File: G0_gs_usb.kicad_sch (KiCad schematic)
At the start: 54 parts, among them J1 USB_C_Receptacle_USB2.0, J12 CAN1, J13 CAN2, J4 Conn_01x03_Pin, U1 STM32G0B1CBTx, U2 TJA1042T-3, U3 TJA1042T-3, U4 XC6206PxxxMR

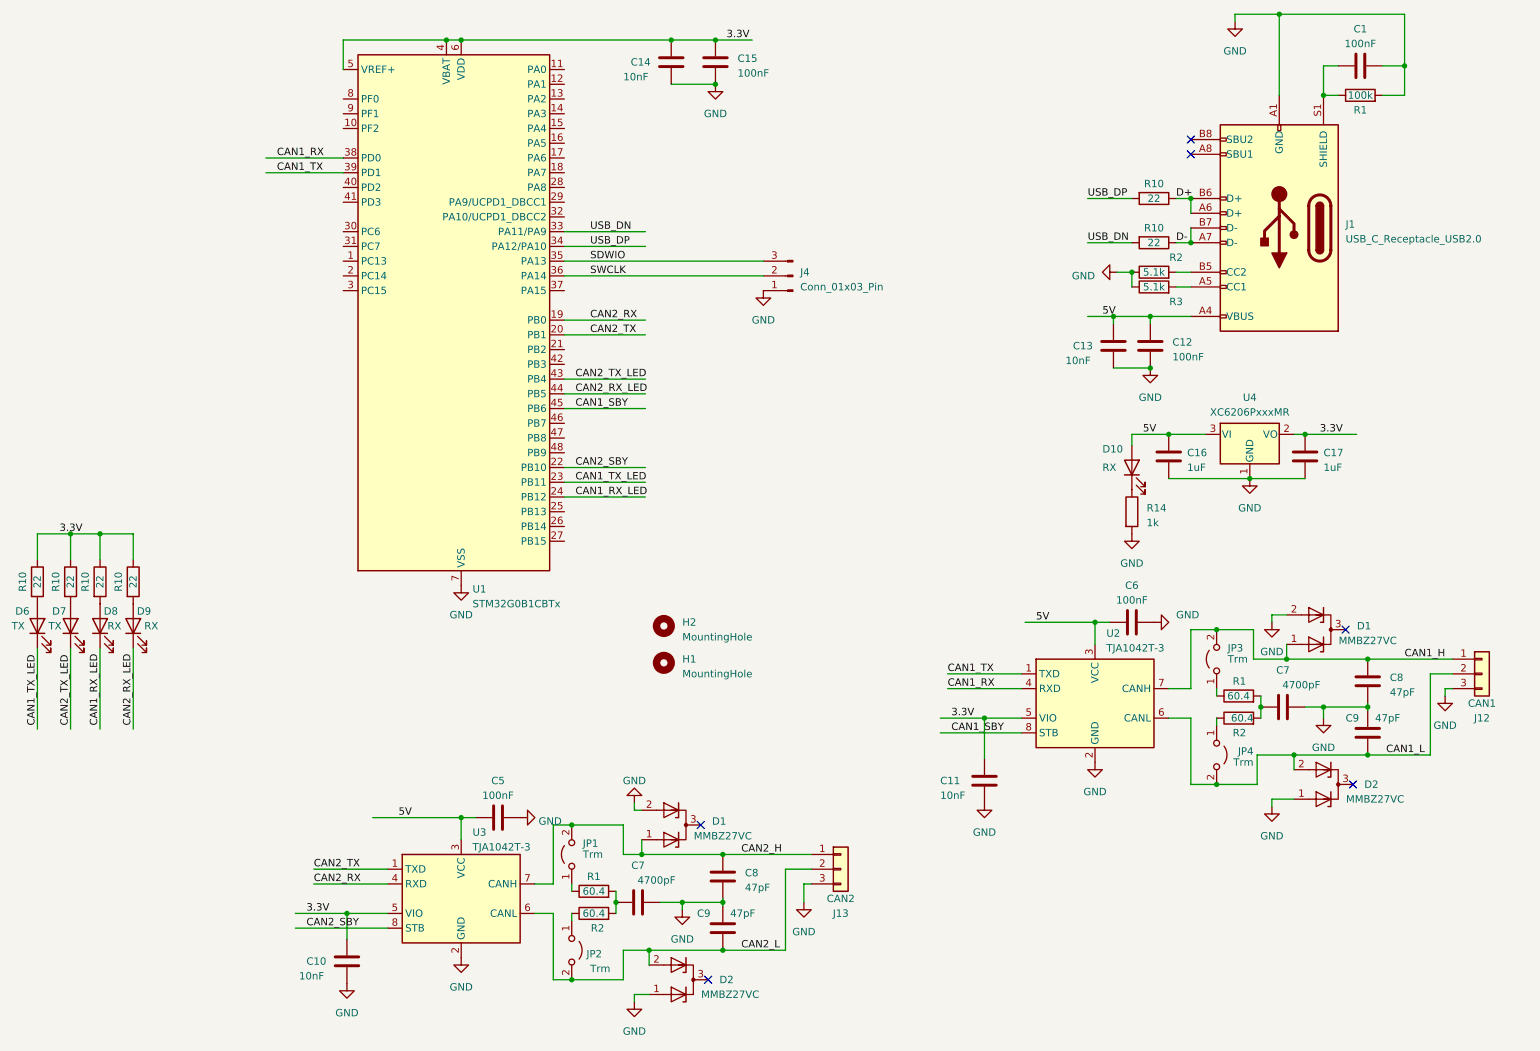
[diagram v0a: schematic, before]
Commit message: Update footprints on R and C to 0402. Added 5V protection. Routed CAN RX/TX as diff pairs.
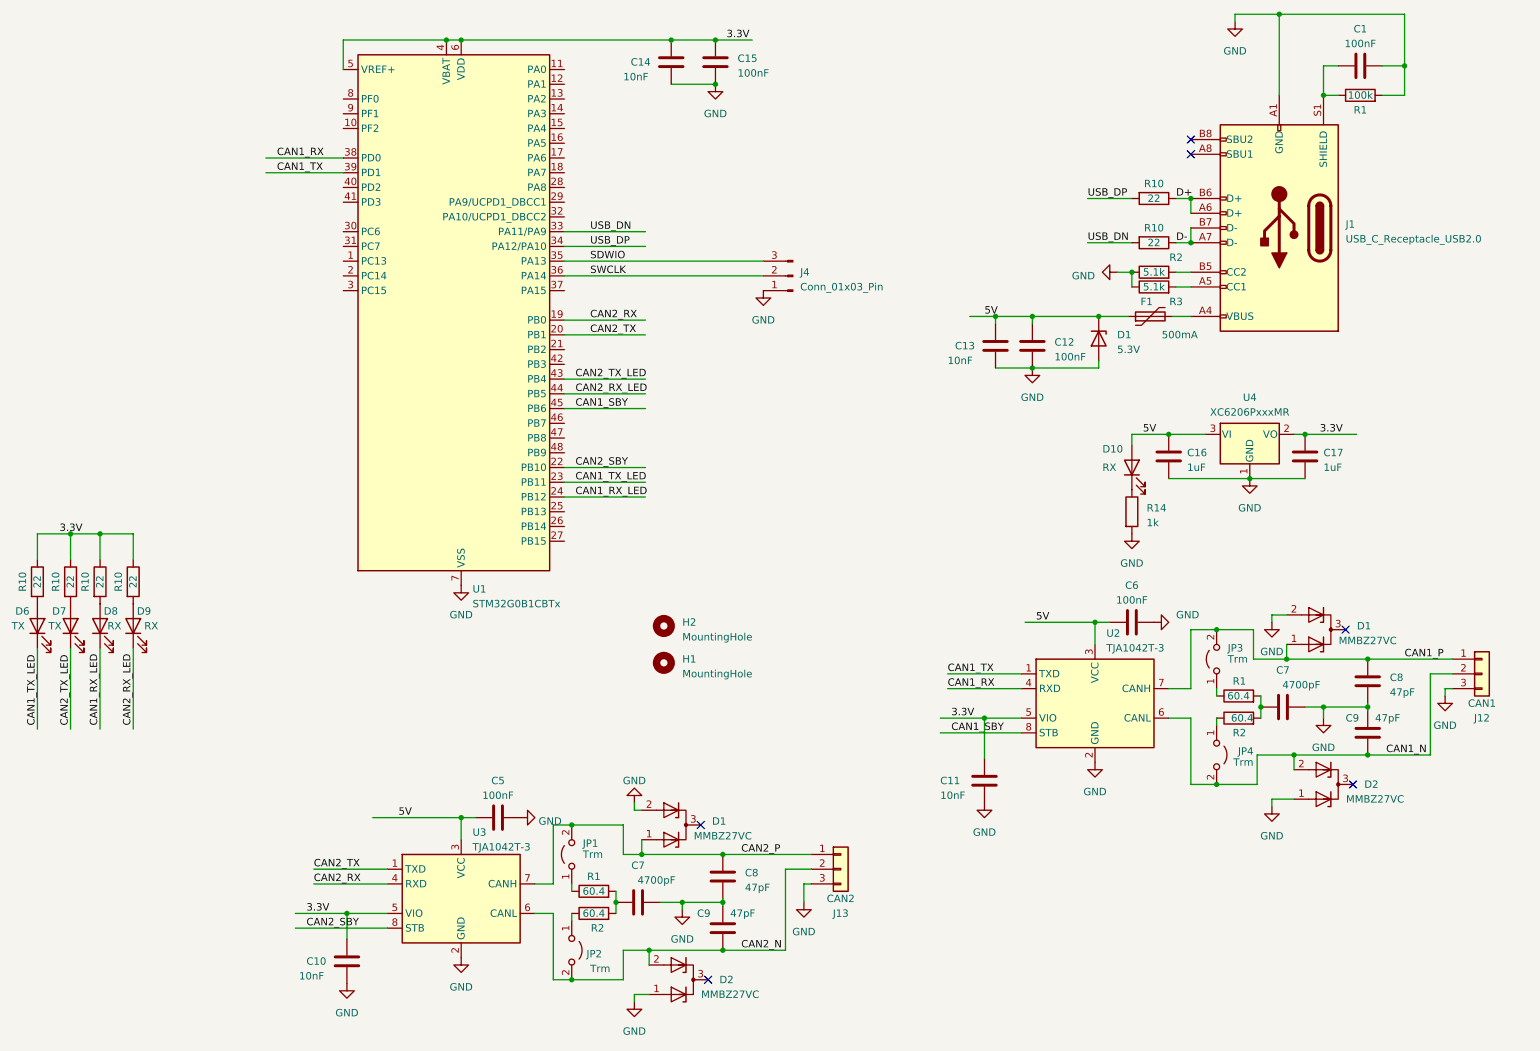
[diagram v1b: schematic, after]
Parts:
- added D1: 5.3V, Diode_SMD:D_MELF, symbol Device:D_Zener
- added F1: 500mA, Fuse:Fuse_0603_1608Metric, symbol Device:Polyfuse
- C1, C12, C15, C5, C6: footprint Capacitor_SMD:C_0603_1608Metric -> Capacitor_SMD:C_0402_1005Metric; LCSC Part # C14663 -> C307331; Part # (none) -> CL05B104KB54PNC
- C10, C11, C13, C14: footprint Capacitor_SMD:C_0603_1608Metric -> Capacitor_SMD:C_0402_1005Metric; LCSC Part # C57112 -> C15195; Part # (none) -> CL05B103KB5NNNC
- C7: footprint Capacitor_SMD:C_0603_1608Metric -> Capacitor_SMD:C_0402_1005Metric; LCSC Part # C53987 -> C1538; Part # (none) -> 0402B472K500NT
- C8, C9: footprint Capacitor_SMD:C_0603_1608Metric -> Capacitor_SMD:C_0402_1005Metric; LCSC Part # C1671 -> C1567; Part # (none) -> 0402CG470J500NT
- R1, R2: footprint Resistor_SMD:R_0603_1608Metric -> Resistor_SMD:R_0402_1005Metric; LCSC Part # C23090 -> C11616; Part # (none) -> 0402WGF5103TCE
- R1: footprint Resistor_SMD:R_0603_1608Metric -> Resistor_SMD:R_0402_1005Metric; LCSC Part # C25803 -> C11616; Part # (none) -> 0402WGF5103TCE
- R10: footprint Resistor_SMD:R_0603_1608Metric -> Resistor_SMD:R_0402_1005Metric; LCSC Part # C23345 -> C25092; Part # 0603WAF220JT5E -> 0402WGF220JTCE
- R2, R3: footprint Resistor_SMD:R_0603_1608Metric -> Resistor_SMD:R_0402_1005Metric; LCSC Part # C23186 -> C11616; Part # (none) -> 0402WGF5103TCE
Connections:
- net 5V: now also D1.1 (K), F1.1; no longer J1.A4 (VBUS), J1.A9 (VBUS), J1.B4 (VBUS), J1.B9 (VBUS)
- net GND: now also D1.2 (A)
- net CAN1_H renamed CAN1_P
- net CAN1_L renamed CAN1_N
- net CAN2_H renamed CAN2_P
- net CAN2_L renamed CAN2_N
- new net: F1.2, J1.A4 (VBUS), J1.A9 (VBUS), J1.B4 (VBUS), J1.B9 (VBUS)
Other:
- moved on the sheet: C12, C13

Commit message: Use better TVS diodes.
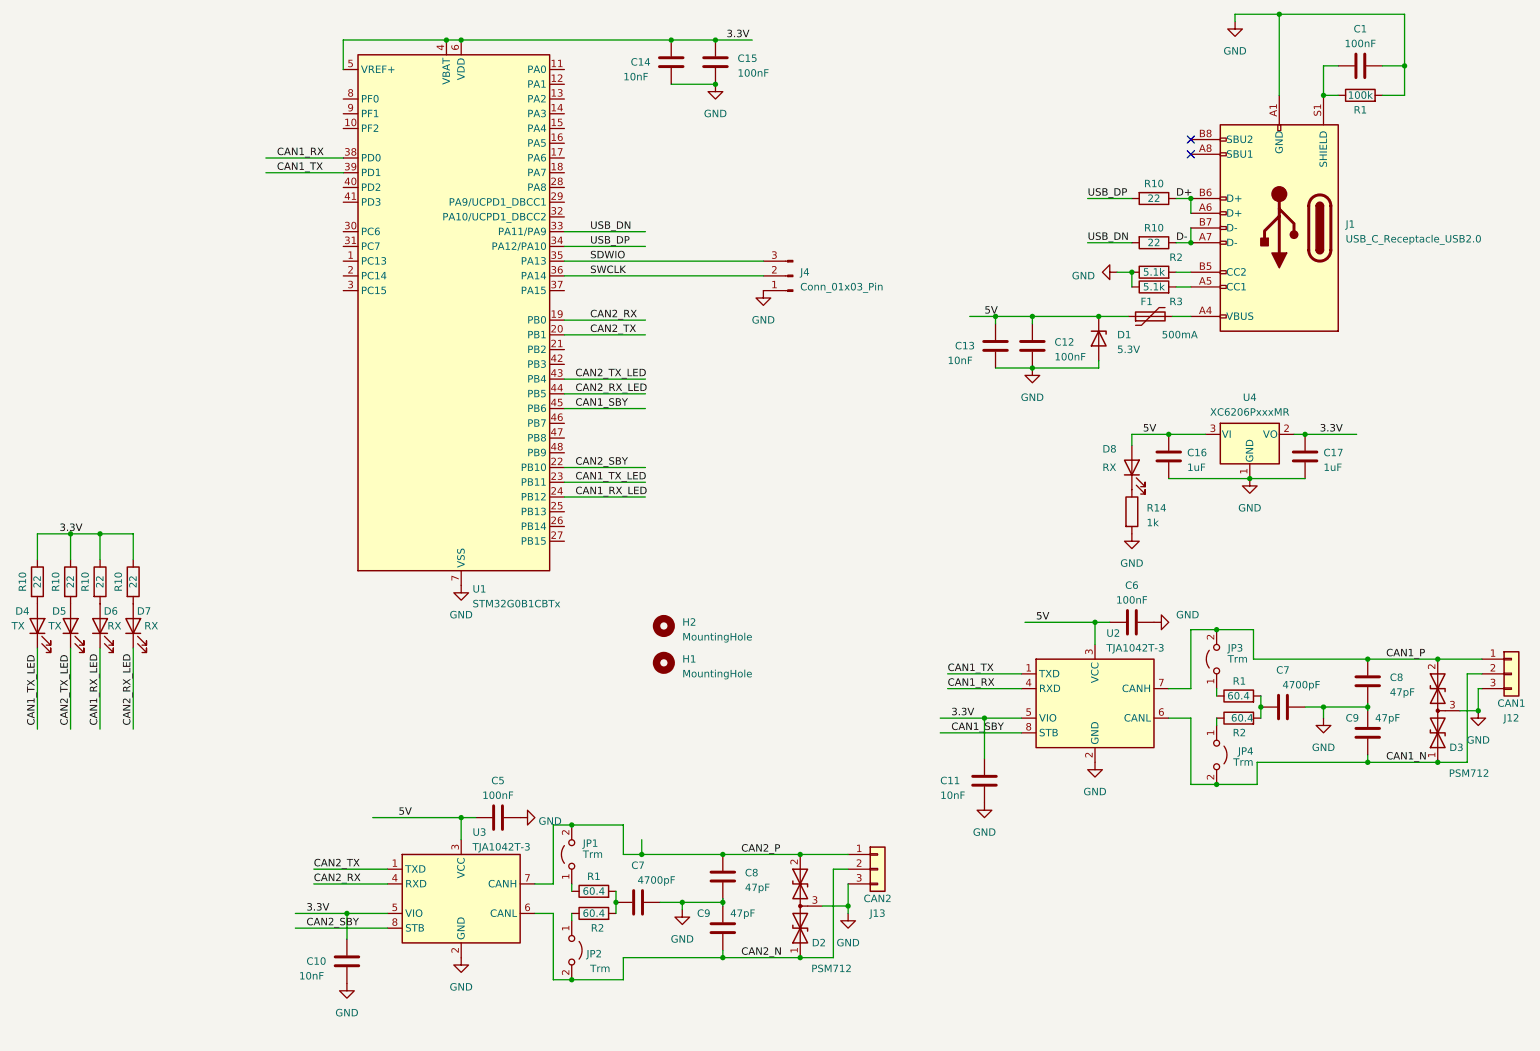
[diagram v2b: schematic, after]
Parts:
- removed D1 (x2), D2 (x2): MMBZ27VC, Package_TO_SOT_SMD:SOT-23, symbol ESD:MMBZxxVC
- added D2, D3: PSM712, Package_TO_SOT_SMD:SOT-23-3, symbol Device:D_TVS_Dual_AAC
- R1, R2: LCSC Part # C11616 -> C137954; Part # 0402WGF5103TCE -> RC0402FR-0760R4L
- R1: LCSC Part # C11616 -> C25741; Part # 0402WGF5103TCE -> 0402WGF1003TCE
- R14: Part # (none) -> 0402WGF1001TCE
- renumbered D6 to D4, D7 to D5, D8 to D6, D9 to D7, D10 to D8
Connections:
- net CAN1_N: now also D3.1 (A1)
- net CAN1_P: now also D3.2 (A2)
- net CAN2_N: now also D2.1 (A1)
- net CAN2_P: now also D2.2 (A2)
- net GND: now also D2.3 (common), D3.3 (common)
- no-connect marks 6 -> 2
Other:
- moved on the sheet: J12, J13

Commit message: Update TVS diodes. Add reset button.
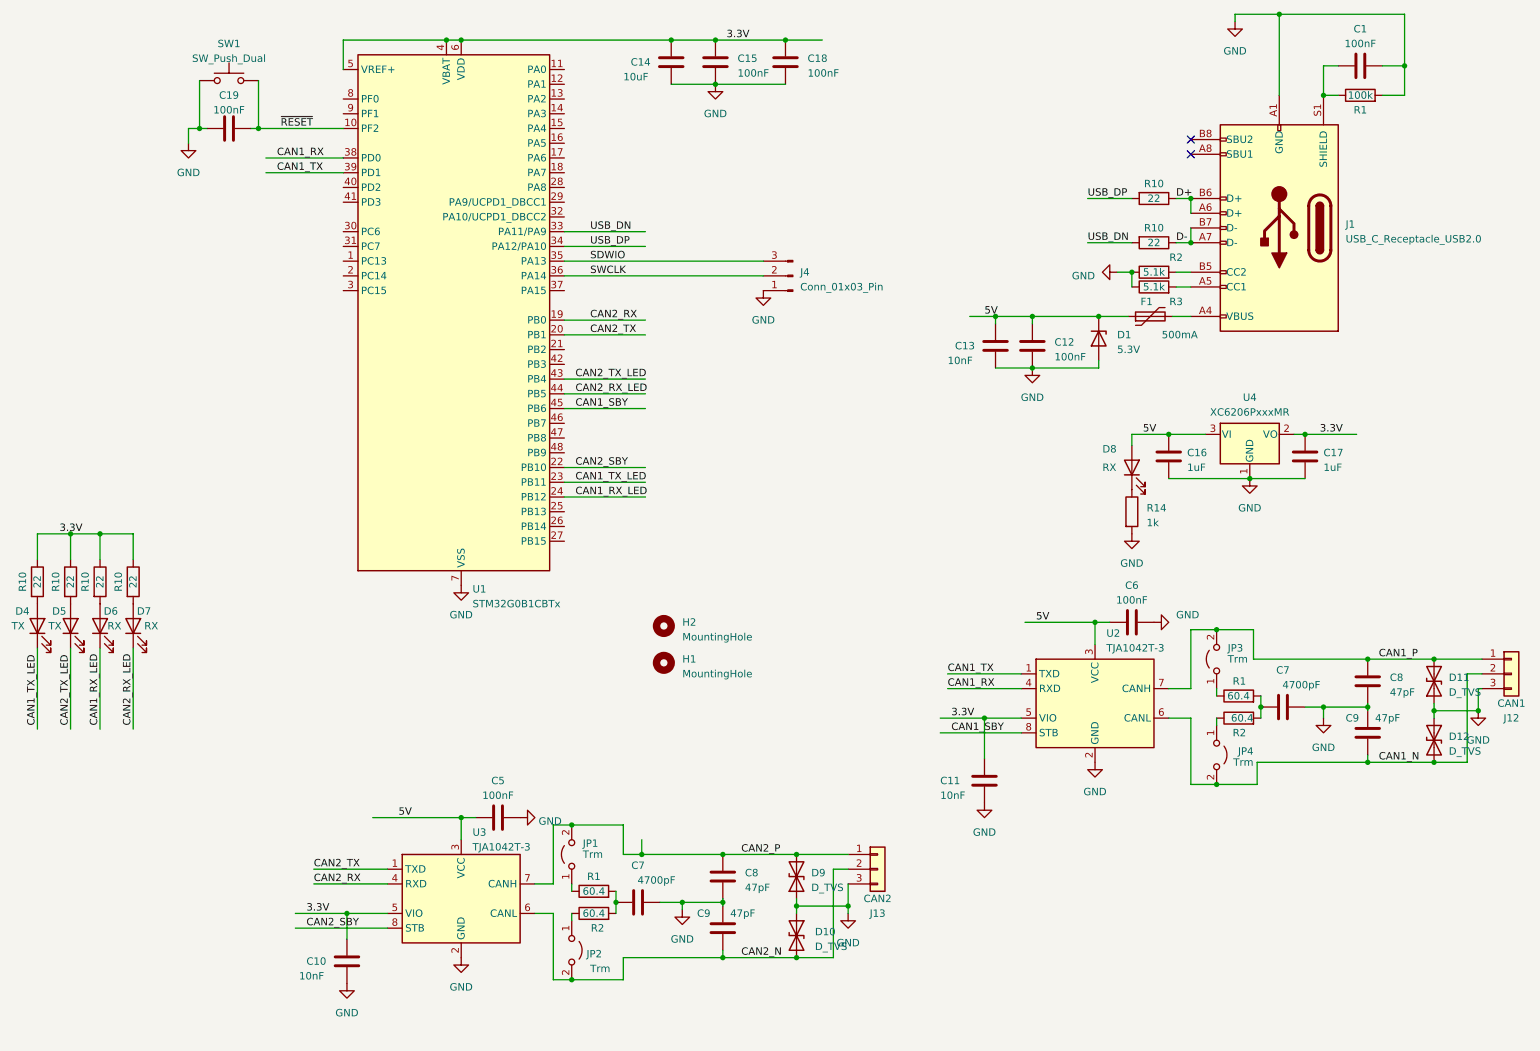
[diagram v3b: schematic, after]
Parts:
- removed D2, D3: PSM712, Package_TO_SOT_SMD:SOT-23-3, symbol Device:D_TVS_Dual_AAC
- added C18, C19: 100nF, Capacitor_SMD:C_0402_1005Metric, symbol Device:C
- added D10, D11, D12, D9: D_TVS, Diode_SMD:D_SOD-123F, symbol Device:D_TVS
- added SW1: SW_Push_Dual, Button_Switch_SMD:SW_SPST_TL3342, symbol Switch:SW_Push
- C14: value 10nF -> 10uF; footprint Capacitor_SMD:C_0402_1005Metric -> Capacitor_SMD:C_0603_1608Metric; LCSC Part # C15195 -> C96446; Part # CL05B103KB5NNNC -> CL10A106MA8NRNC
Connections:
- net 3.3V: now also C18.2
- net CAN1_N: now also D12.2 (A2)
- net CAN1_P: now also D11.2 (A2)
- net CAN2_N: now also D10.2 (A2)
- net CAN2_P: now also D9.2 (A2)
- net GND: now also C18.1, C19.2, D10.1 (A1), D11.1 (A1), D12.1 (A1), D9.1 (A1), SW1.1
- net ~{RESET}: now reaches U1.10 (PF2)
- net ~{RESET}: now also C19.1, SW1.2
